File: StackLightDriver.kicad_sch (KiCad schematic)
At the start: 52 parts, among them J1 Conn_01x02_Pin, J10 Conn_01x02_Pin, J11 Barrel_Jack_Switch, J2 Conn_01x02_Pin, J3 Conn_01x02_Pin, J4 Conn_01x02_Pin, J5 Conn_01x02_Pin, J6 Conn_01x02_Pin, J7 Conn_01x02_Pin, J8 Conn_01x02_Pin, J9 Conn_01x02_Pin, P1 282837-2, P2 282837-2, P3 282837-2, U6 ESP32-S3-WROOM-1-N4

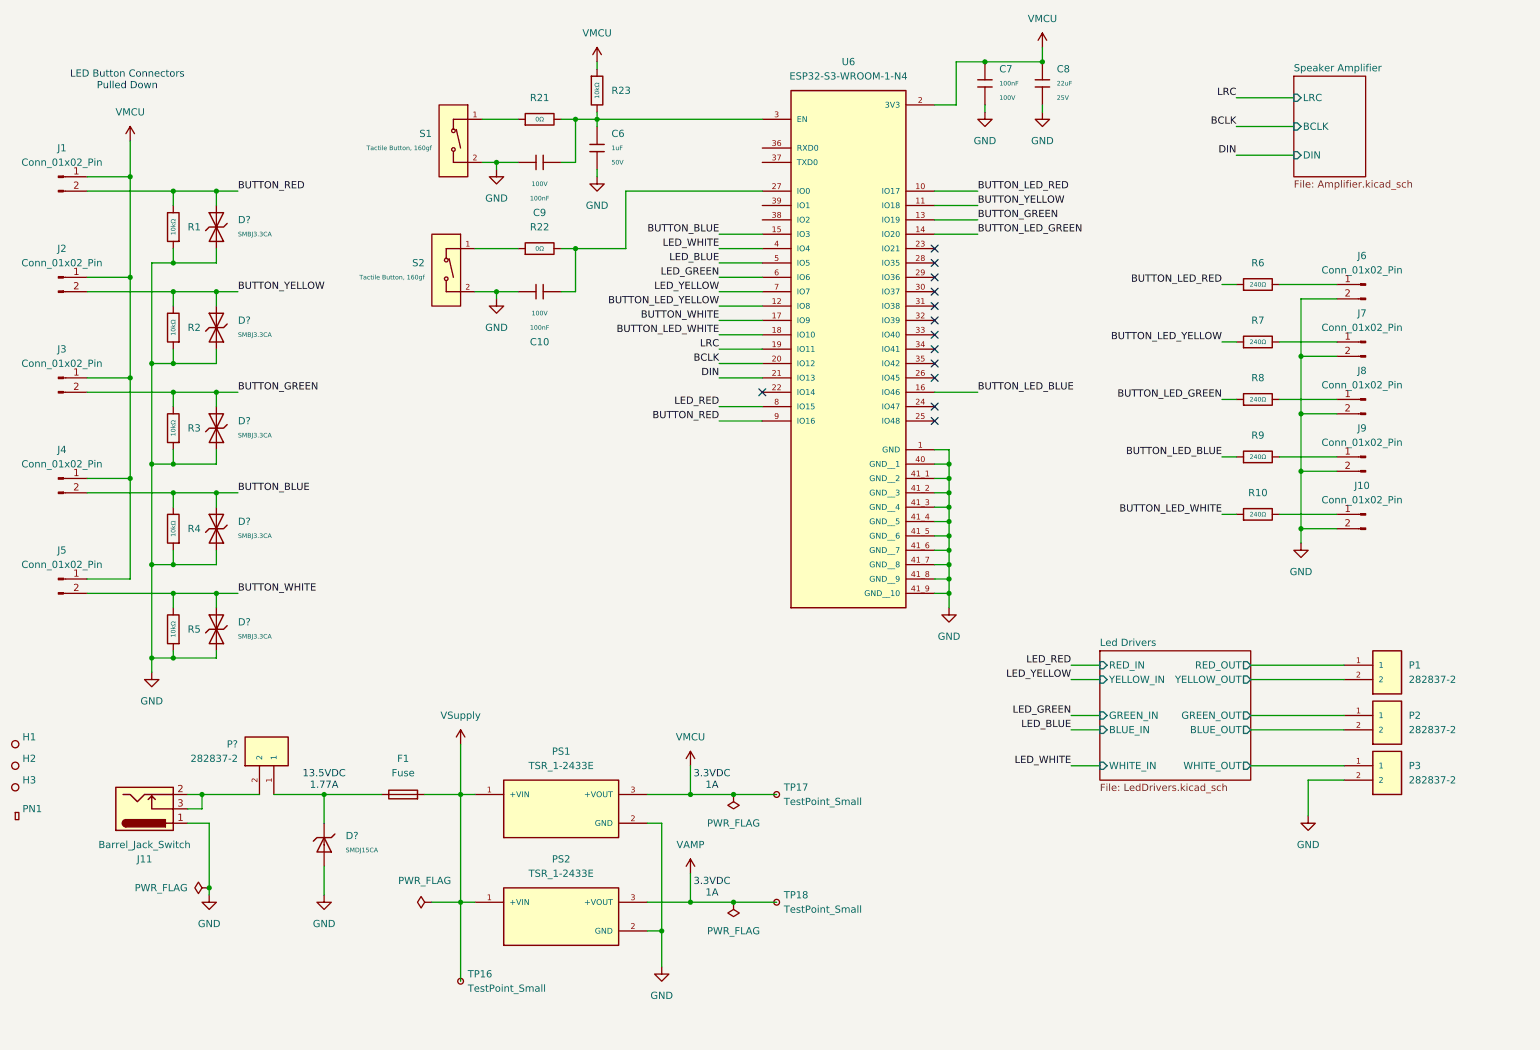
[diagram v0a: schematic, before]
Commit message: Recreated symbol/footprint libraries, added 3D models and Git LFS
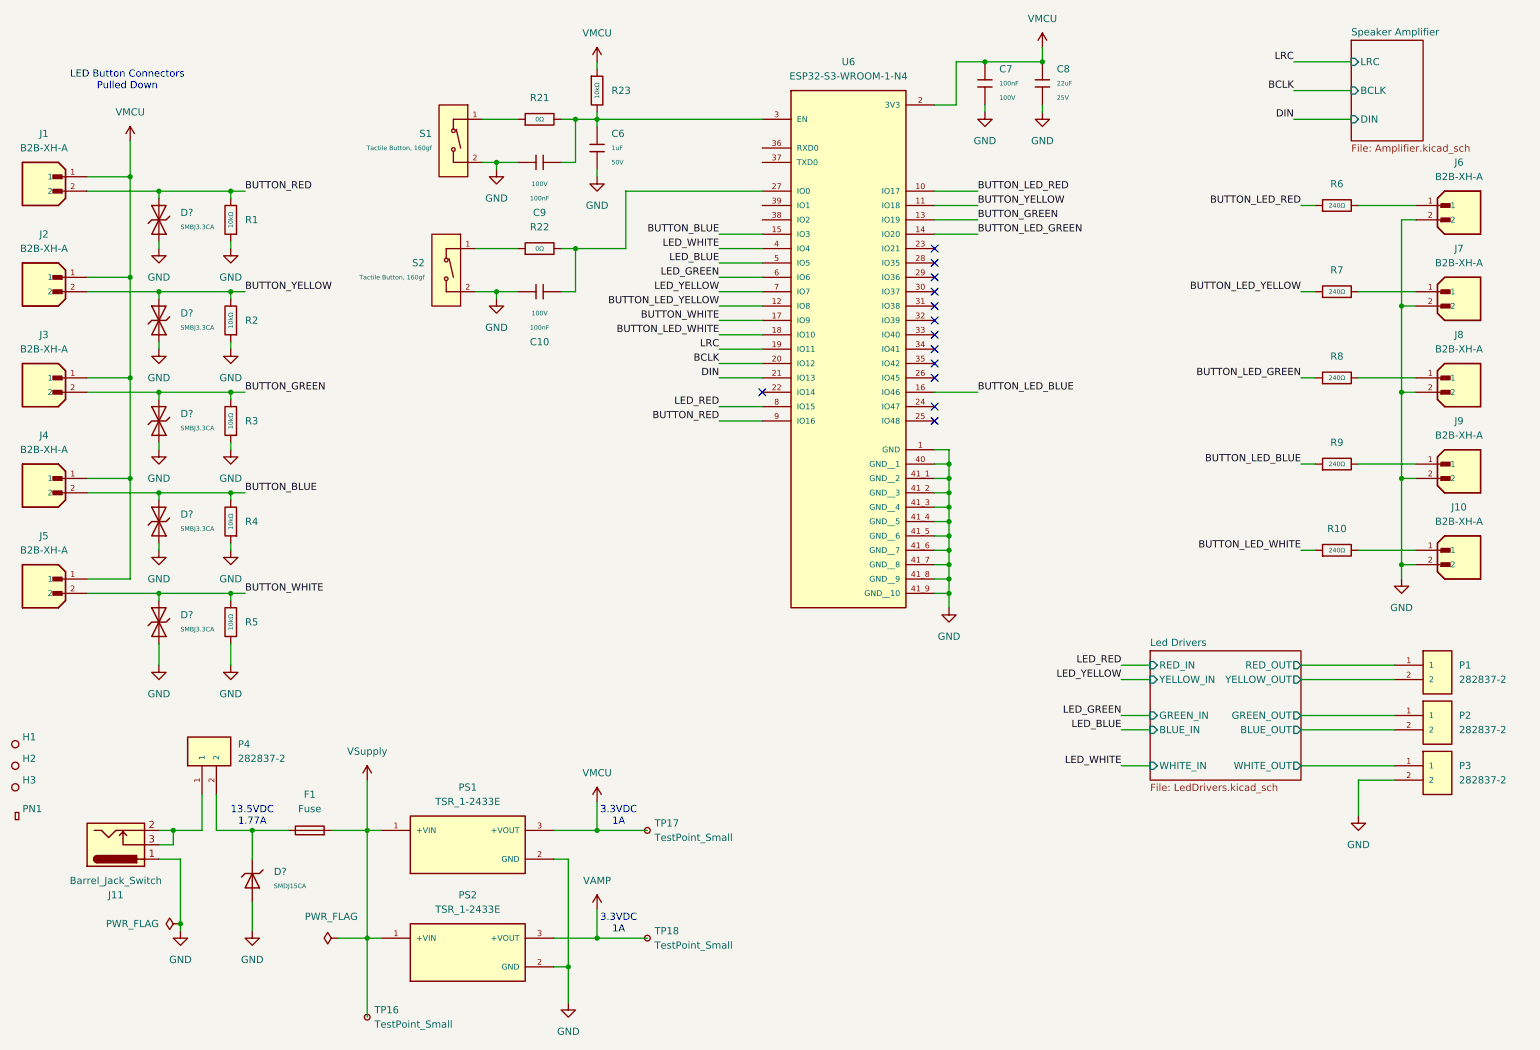
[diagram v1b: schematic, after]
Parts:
- removed J1, J10, J2, J3, J4, J5, J6, J7, J8, J9: Conn_01x02_Pin, symbol Connector:Conn_01x02_Pin
- removed P1, P2, P3, P?: 282837-2, 282837-2:TE_282837-2, symbol 282837-2:282837-2
- removed PS1, PS2: TSR_1-2433E, TSR_1-2433E:CONV_TSR_1-2433E, symbol TSR_1-2433E:TSR_1-2433E
- removed U6: ESP32-S3-WROOM-1-N4, ESP32-S3-WROOM-1-N4:XCVR_ESP32-S3-WROOM-1-N4, symbol ESP32-S3-WROOM-1-N4:ESP32-S3-WROOM-1-N4
- added J1, J10, J2, J3, J4, J5, J6, J7, J8, J9: B2B-XH-A, Project_footprints:JST_B2B-XH-A, symbol Project_symbols:B2B-XH-A
- added P1, P2, P3, P4: 282837-2, Project_footprints:TE_282837-2, symbol Project_symbols:282837-2
- added PS1, PS2: TSR_1-2433E, Project_footprints:CONV_TSR_1-2433E, symbol Project_symbols:TSR_1-2433E
- added U6: ESP32-S3-WROOM-1-N4, Project_footprints:XCVR_ESP32-S3-WROOM-1-N4, symbol Project_symbols:ESP32-S3-WROOM-1-N4
- F1: footprint (none) -> Fuse:Fuseholder_Clip-5x20mm_Littelfuse_111_Lateral_P18.80x5.00mm_D1.17mm_Horizontal
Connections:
- net BCLK: now also U6.20 (IO12)
- net BUTTON_BLUE: now also J4.2, U6.15 (IO3)
- net BUTTON_GREEN: now also J3.2, U6.13 (IO19)
- net BUTTON_LED_BLUE: now also U6.16 (IO46)
- net BUTTON_LED_GREEN: now also U6.14 (IO20)
- net BUTTON_LED_RED: now also U6.10 (IO17)
- net BUTTON_LED_WHITE: now also U6.18 (IO10)
- net BUTTON_LED_YELLOW: now also U6.12 (IO8)
- net BUTTON_RED: now also J1.2, U6.9 (IO16)
- net BUTTON_WHITE: now also J5.2, U6.17 (IO9)
- net BUTTON_YELLOW: now also J2.2, U6.11 (IO18)
- net DIN: now also U6.21 (IO13)
- net GND: now also J10.2, J6.2, J7.2, J8.2, J9.2, P3.2, PS1.2 (GND), PS2.2 (GND), U6.1 (GND), U6.40 (GND__1), U6.41_1 (GND__2), U6.41_2 (GND__3), U6.41_3 (GND__4), U6.41_4 (GND__5), U6.41_5 (GND__6), U6.41_6 (GND__7), U6.41_7 (GND__8), U6.41_8 (GND__9), U6.41_9 (GND__10)
- net LED_BLUE: now also U6.5 (IO5)
- net LED_GREEN: now also U6.6 (IO6)
- net LED_RED: now also U6.8 (IO15)
- net LED_WHITE: now also U6.4 (IO4)
- net LED_YELLOW: now also U6.7 (IO7)
- net LRC: now also U6.19 (IO11)
- net Led Drivers/BLUE_OUT: now also P2.2
- net Led Drivers/GREEN_OUT: now also P2.1
- net Led Drivers/RED_OUT: now also P1.1
- net Led Drivers/WHITE_OUT: now also P3.1
- net Led Drivers/YELLOW_OUT: now also P1.2
- net VAMP: now also PS2.3 (+VOUT)
- net VMCU: now also J1.1, J2.1, J3.1, J4.1, J5.1, PS1.3 (+VOUT), U6.2 (3V3)
- net VSupply: now also PS1.1 (+VIN), PS2.1 (+VIN)
- net at R8.2: now also J8.1
- net at R7.2: now also J7.1
- net at D?.1, F1.1: now also P4.2
- net at C6.1, C9.2, R21.2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: now also U6.3 (EN)
- net at C10.2, R22.2: now also U6.27 (IO0)
- net at R10.2: now also J10.1
- net at J11.2, J11.3: now also P4.1
- net at R6.2: now also J6.1
- net at R9.2: now also J9.1
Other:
- moved on the sheet: D?, F1, J11, R1, R10, R2, R3, R4, R5, R6, R7, R8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

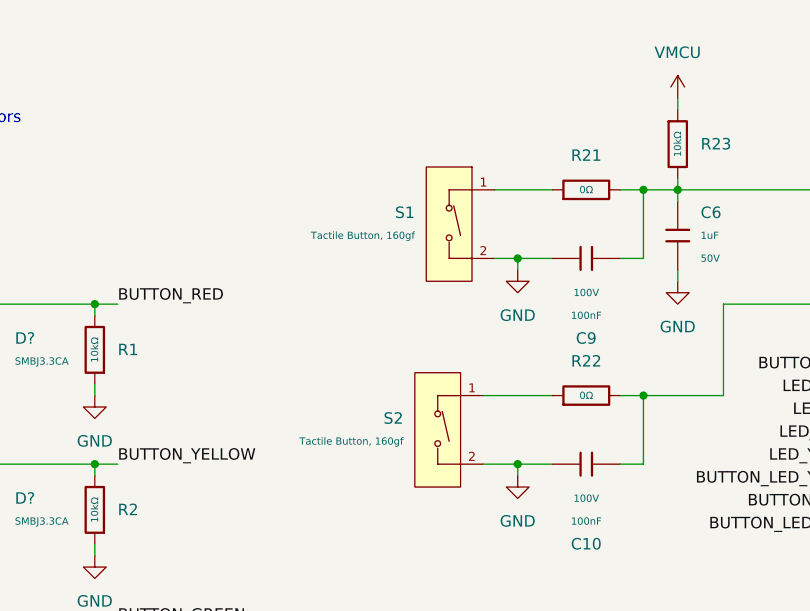
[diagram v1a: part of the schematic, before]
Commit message: Copied PCM_JLCPCB tactile switch symbol to change pins to passive for ERC
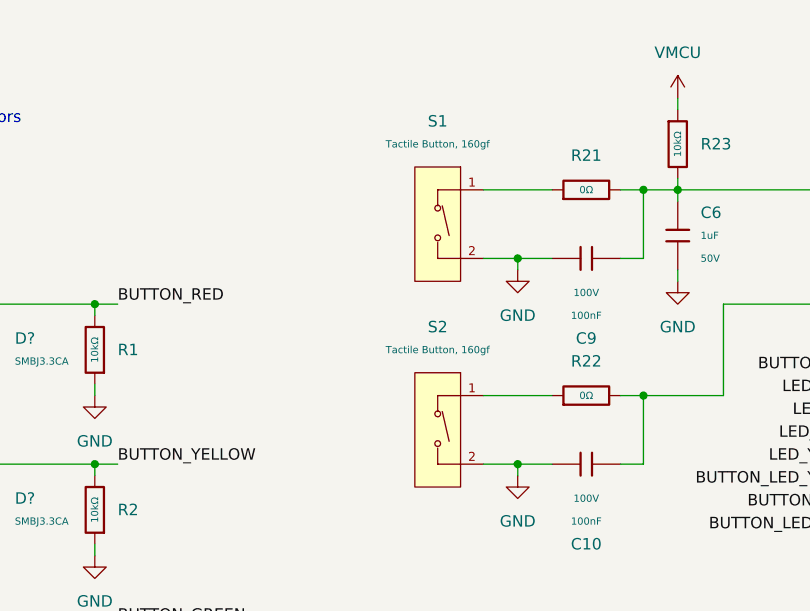
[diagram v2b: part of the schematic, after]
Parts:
- removed S1, S2: Tactile Button, 160gf, PCM_JLCPCB:SW_TS-1088-AR02016, symbol PCM_JLCPCB-Connectors_Buttons:Tactile Button, 160gf, 12V, 50mA, 4.0mm
- added S1, S2: Tactile Button, 160gf, PCM_JLCPCB:SW_TS-1088-AR02016, symbol Project_symbols:Tactile Button, 160gf, 12V, 50mA, 4.0mm
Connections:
- net GND: now also S1.2 (B), S2.2 (B)
- net at R21.1: now also S1.1 (A)
- net at R22.1: now also S2.1 (A)

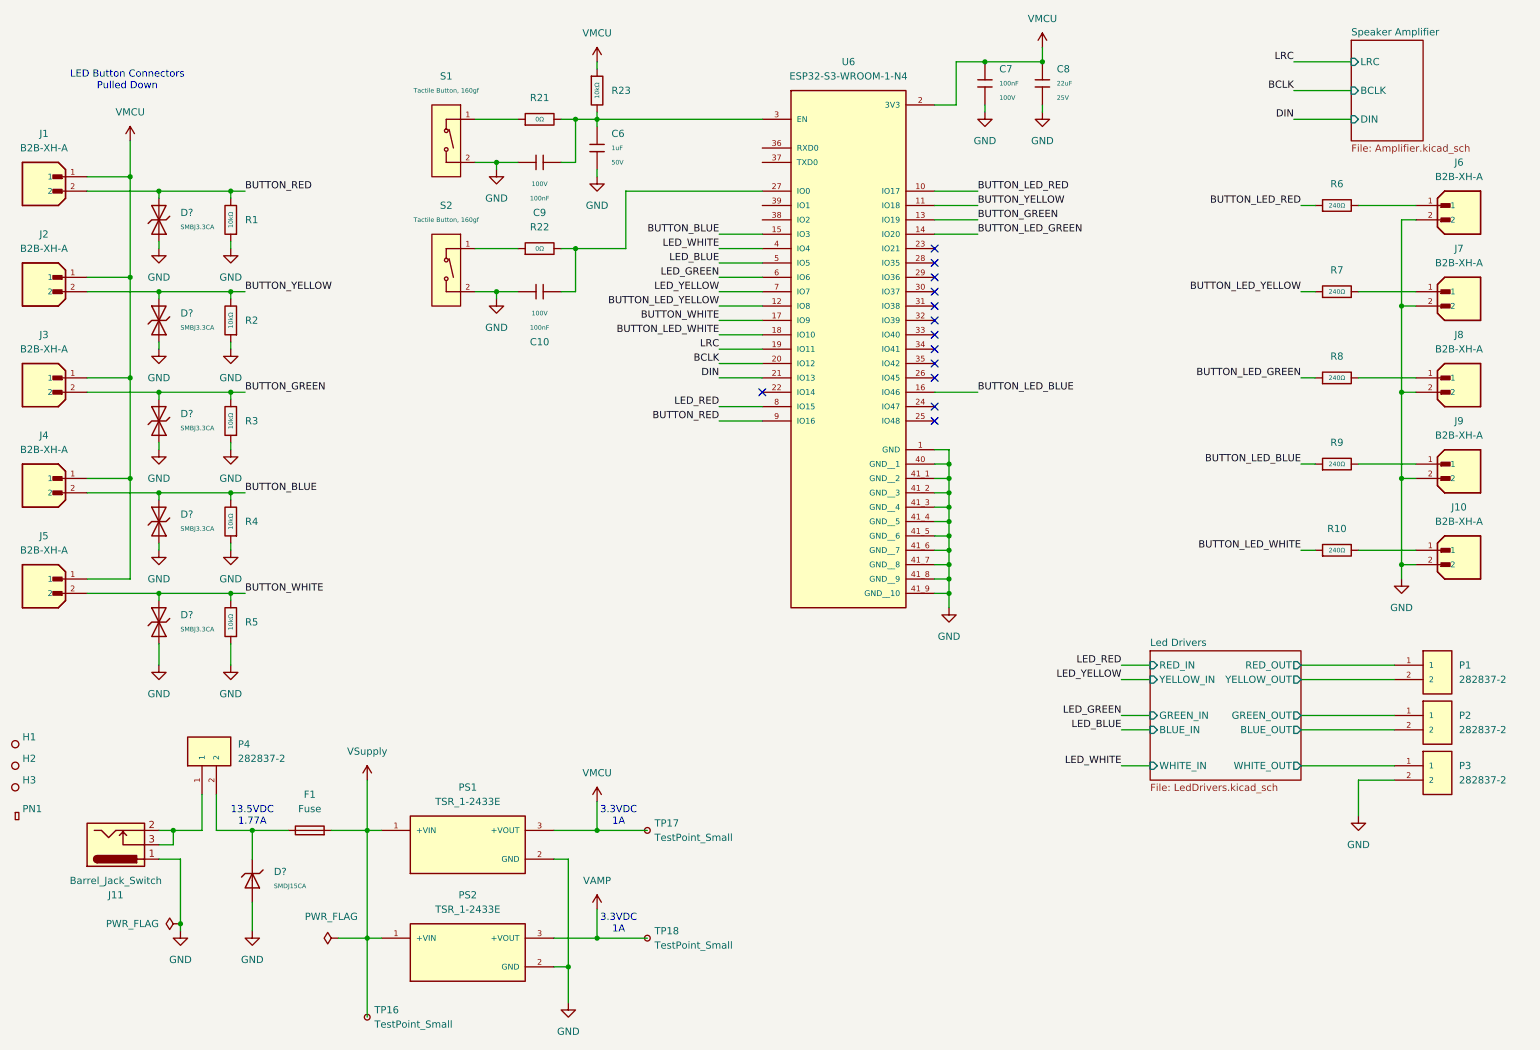
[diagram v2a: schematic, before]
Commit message: Added 3D model and footprint for power jack
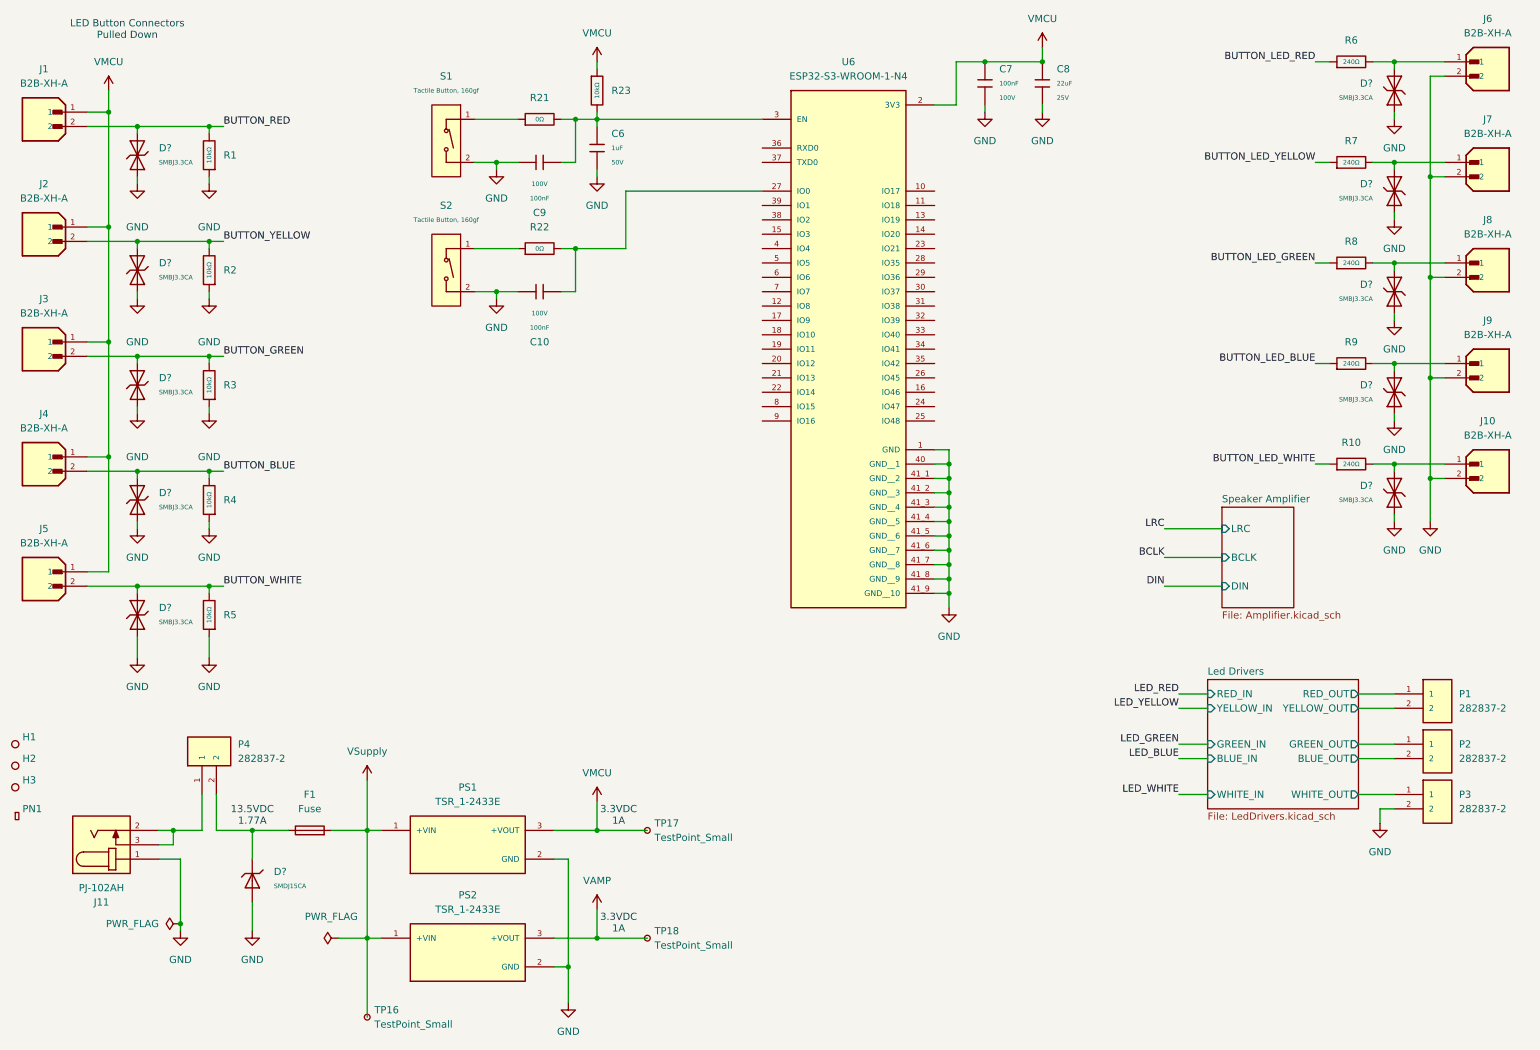
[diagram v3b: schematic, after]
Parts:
- removed J11: Barrel_Jack_Switch, symbol Connector:Barrel_Jack_Switch
- added D? (x5): SMBJ3.3CA, PCM_JLCPCB:D_SMB, symbol PCM_JLCPCB-Diodes:TVS-Bi,SMBJ3.3CA
- added J11: PJ-102AH, Project_footprints:CUI_PJ-102AH, symbol Project_symbols:PJ-102AH
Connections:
- net BCLK: no longer U6.20 (IO12)
- net BUTTON_BLUE: no longer U6.15 (IO3)
- net BUTTON_GREEN: no longer U6.13 (IO19)
- net BUTTON_LED_BLUE: no longer U6.16 (IO46)
- net BUTTON_LED_GREEN: no longer U6.14 (IO20)
- net BUTTON_LED_RED: no longer U6.10 (IO17)
- net BUTTON_LED_WHITE: no longer U6.18 (IO10)
- net BUTTON_LED_YELLOW: no longer U6.12 (IO8)
- net BUTTON_RED: no longer U6.9 (IO16)
- net BUTTON_WHITE: no longer U6.17 (IO9)
- net BUTTON_YELLOW: no longer U6.11 (IO18)
- net DIN: no longer U6.21 (IO13)
- net GND: now also D?.1, D?.1, D?.1, D?.1, D?.1, J11.1
- net LED_BLUE: no longer U6.5 (IO5)
- net LED_GREEN: no longer U6.6 (IO6)
- net LED_RED: no longer U6.8 (IO15)
- net LED_WHITE: no longer U6.4 (IO4)
- net LED_YELLOW: no longer U6.7 (IO7)
- net LRC: no longer U6.19 (IO11)
- net at J8.1, R8.2: now also D?.2
- net at P4.1: now also J11.2, J11.3
- net at J10.1, R10.2: now also D?.2
- net at J9.1, R9.2: now also D?.2
- net at J7.1, R7.2: now also D?.2
- net at J6.1, R6.2: now also D?.2
- no-connect marks 13 -> 0
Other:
- moved on the sheet: D?, J1, J10, J2, J3, J4, J5, J6, J7, J8, J9, P1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
